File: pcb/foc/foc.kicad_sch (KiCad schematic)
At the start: 29 parts, among them J1 Conn_01x05_Pin, J2 Conn_01x03_Pin, Q1 BTN8982TA, Q2 BTN8982TA, Q3 BTN8982TA, U1 INA240A2PW, U2 INA240A2PW

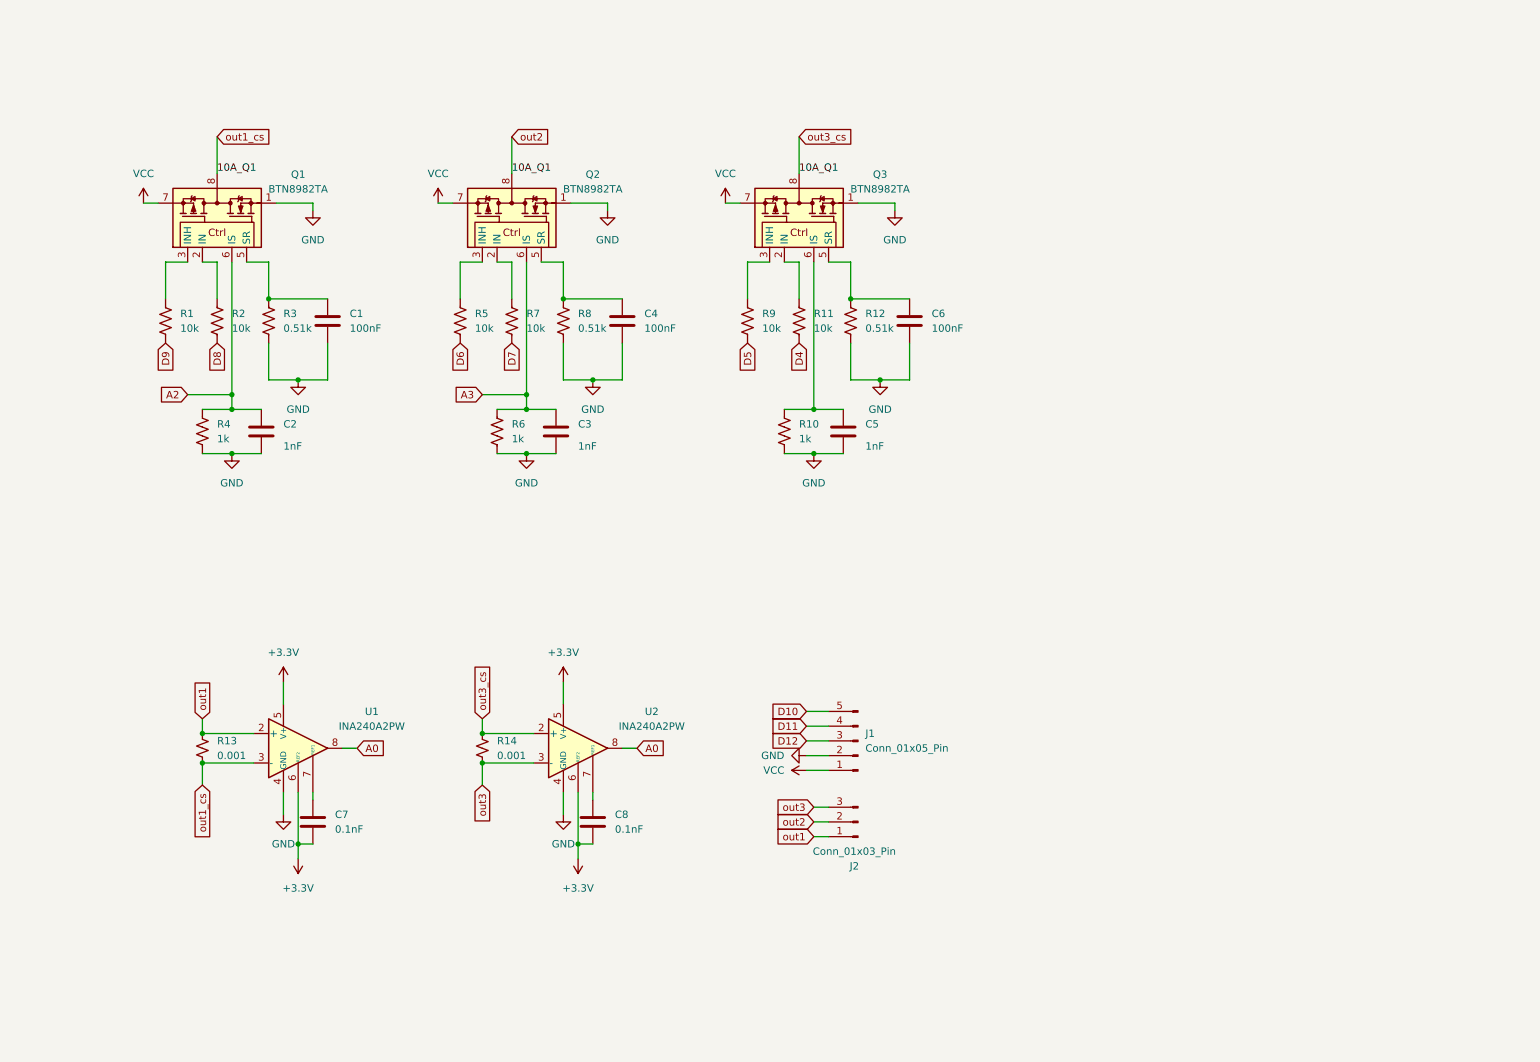
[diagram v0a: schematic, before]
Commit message: update foc board
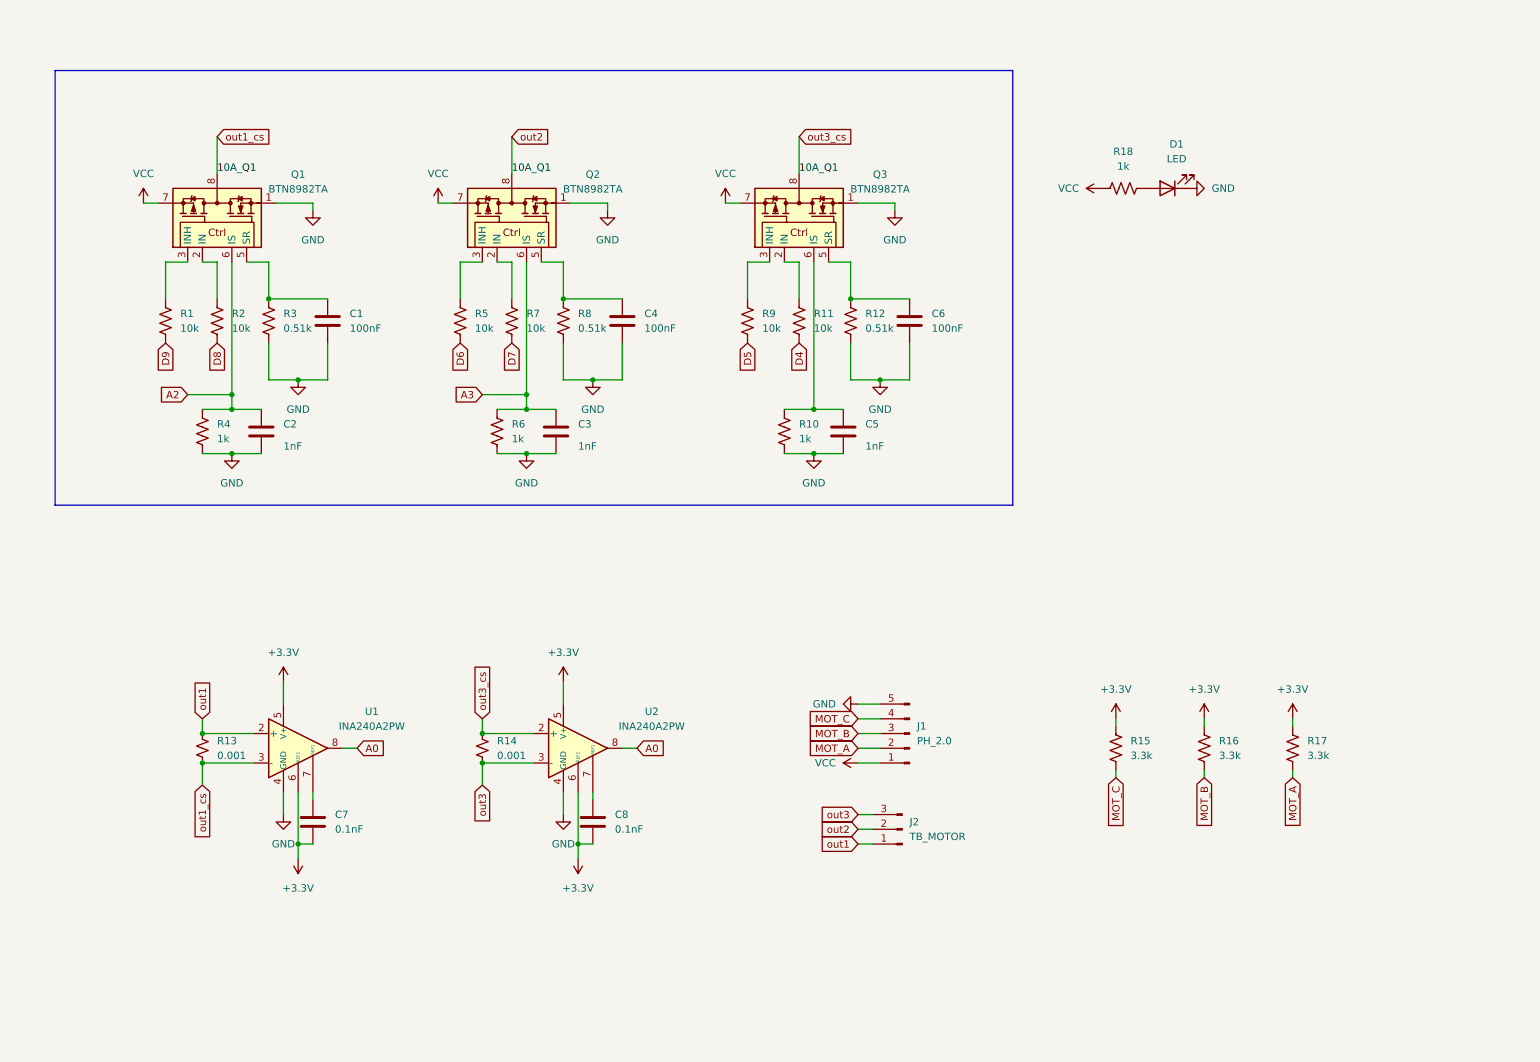
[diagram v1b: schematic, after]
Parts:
- added D1: LED, symbol Device:LED
- added R15, R16, R17: 3.3k, symbol Device:R_US
- added R18: 1k, symbol Device:R_US
- J1: value Conn_01x05_Pin -> PH_2.0
- J2: value Conn_01x03_Pin -> TB_MOTOR
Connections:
- net D10 is gone; now on net GND: J1.5 (Pin_5)
- net +3.3V: now also R15.1, R16.1, R17.1
- net GND: now also D1.1 (K); no longer J1.2 (Pin_2)
- net VCC: now also R18.1
- net D11 renamed MOT_C
- net MOT_C: now also R15.2
- net D12 renamed MOT_B
- net MOT_B: now also R16.2
- new net: D1.2 (A), R18.2
- new net MOT_A: J1.2 (Pin_2), R17.2
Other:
- moved on the sheet: J1, J2

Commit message: foc debug info designe
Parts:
- added D2: LED, symbol Device:LED
- added J3: Power42V, symbol Connector:Conn_01x02_Pin
- added J4, J7: Conn_01x05_Pin, symbol Connector:Conn_01x05_Pin
- added J5: Conn_01x04_Pin, symbol Connector:Conn_01x04_Pin
- added J6: Power3.3, symbol Connector:Conn_01x02_Pin
- added R22: 1k, symbol Device:R_US
- R13, R14: footprint (none) -> Resistor_SMD:R_2512_6332Metric
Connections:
- net +3.3V: now also R15.2, R16.2, J6.1 (Pin_1), R22.2; no longer R15.1, R16.1
- net A0: now also J5.4 (Pin_4); no longer U2.8
- net A2: now also J5.2 (Pin_2)
- net A3: now also J5.1 (Pin_1)
- net D4: now also J4.2 (Pin_2)
- net D5: now also J4.3 (Pin_3)
- net D6: now also J4.4 (Pin_4)
- net D7: now also J4.5 (Pin_5)
- net D8: now also J7.1 (Pin_1)
- net D9: now also J7.2 (Pin_2)
- net GND: now also D2.1 (K), J3.2 (Pin_2), J6.2 (Pin_2)
- net MOT_A: now also J7.3 (Pin_3)
- net MOT_B: now also R16.1, J7.4 (Pin_4); no longer R16.2
- net MOT_C: now also R15.1, J7.5 (Pin_5); no longer R15.2
- net VCC: now also J3.1 (Pin_1)
- net out1_cs: no longer J2.2 (Pin_2), Q2.4, Q2.8, Q3.4, Q3.8, R14.1, U2.2 (+)
- new net: D2.2 (A), R22.1
- new net A1: J5.3 (Pin_3), U2.8
- new net D3: J4.1 (Pin_1)
- new net out2: J2.2 (Pin_2), Q2.4, Q2.8
- new net out3_cs: Q3.4, Q3.8, R14.1, U2.2 (+)
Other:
- note added: "Debug info"
- note added: "current info"
- note added: "hall sensor pins"
- note added: "moto pins"
- note added: "power in and out"
- moved on the sheet: C1, C2, C3, C4, C5, C6, C7, C8, D1, J1, J2, Q1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

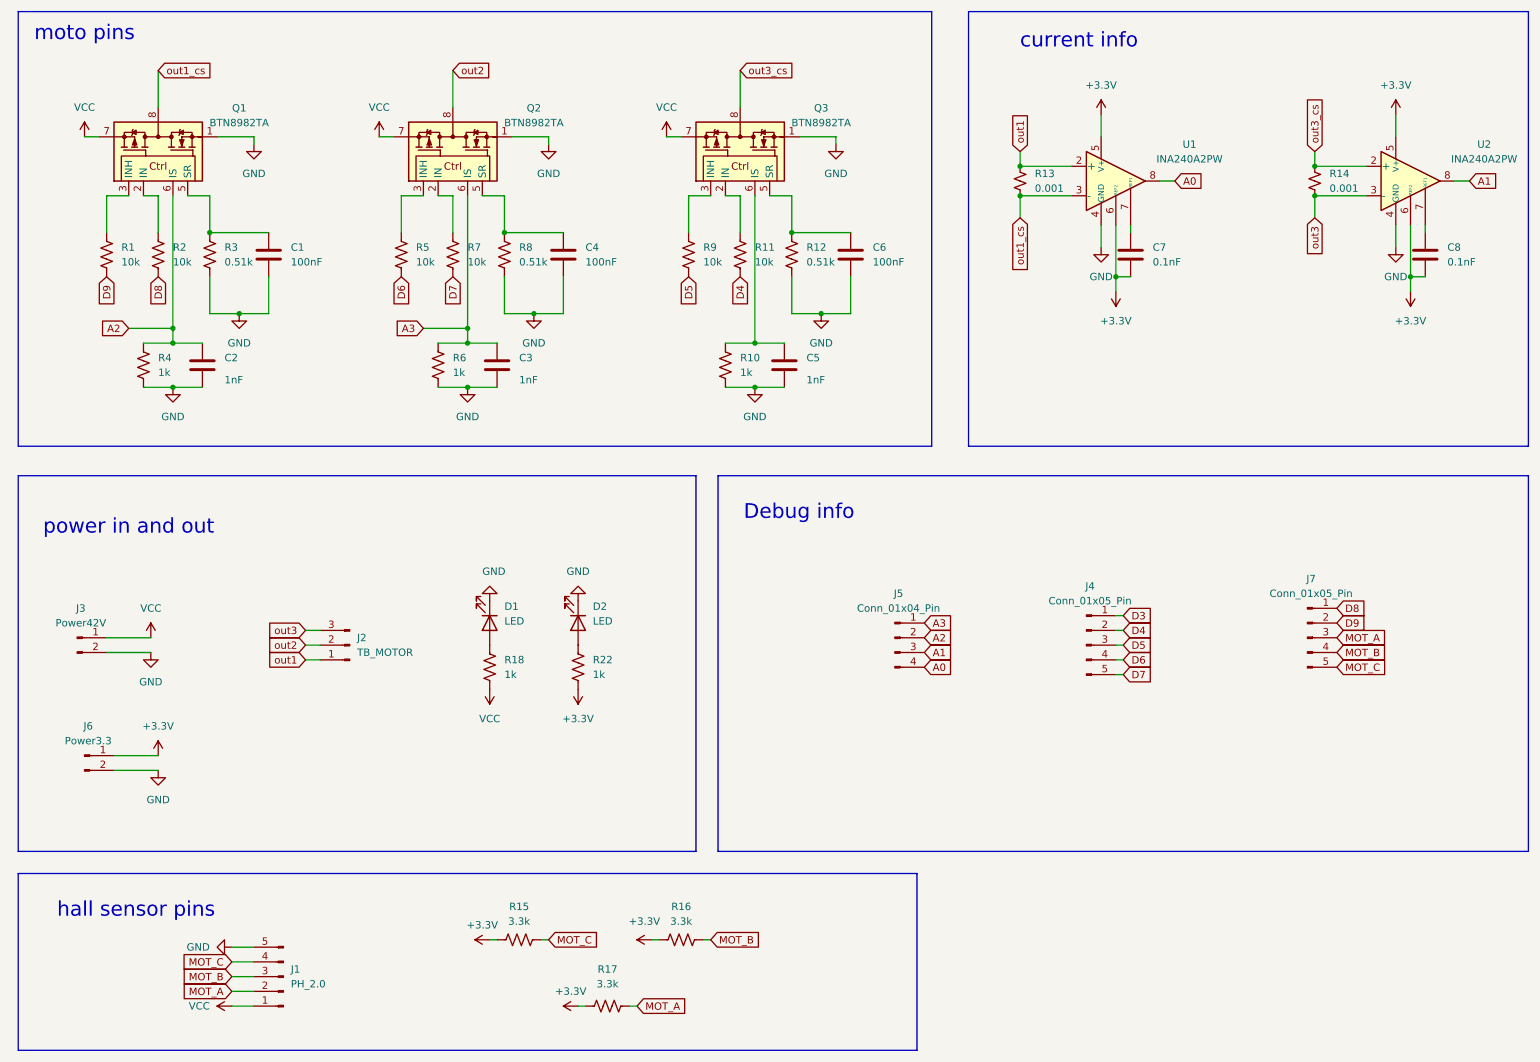
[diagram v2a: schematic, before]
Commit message: assign foot prints
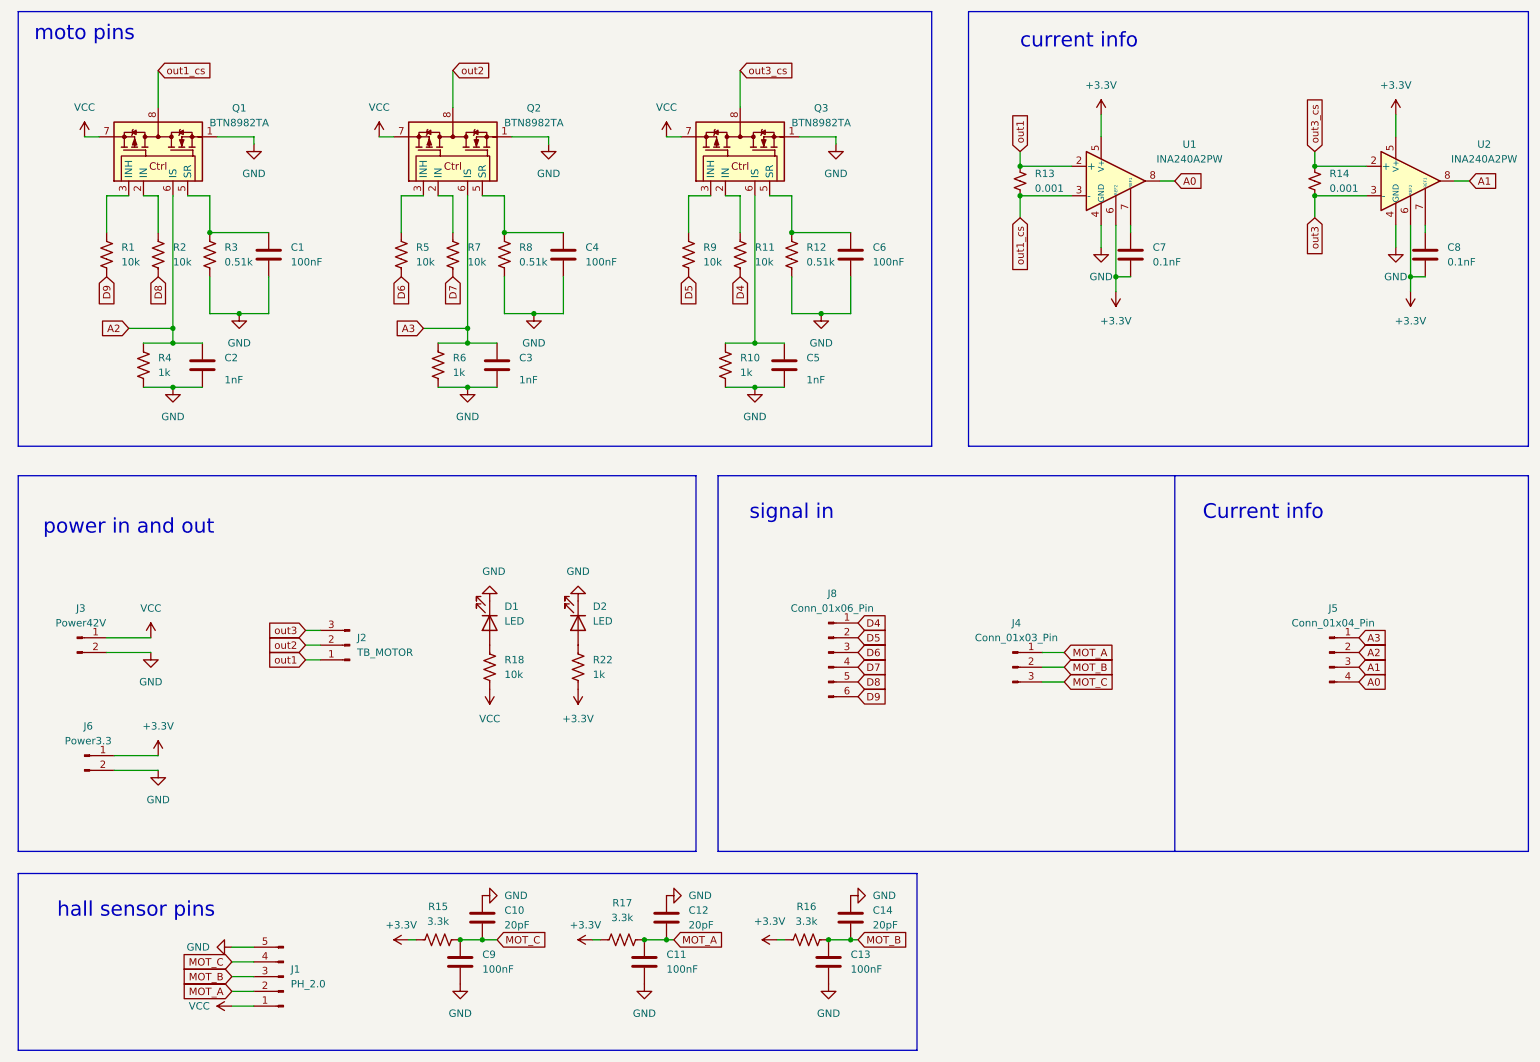
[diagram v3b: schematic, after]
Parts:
- removed J4, J7: Conn_01x05_Pin, symbol Connector:Conn_01x05_Pin
- added C10, C12, C14: 20pF, Capacitor_SMD:C_0603_1608Metric, symbol Device:C
- added C11, C13, C9: 100nF, Capacitor_SMD:C_0603_1608Metric, symbol Device:C
- added J4: Conn_01x03_Pin, Connector_PinHeader_2.54mm:PinHeader_1x03_P2.54mm_Vertical, symbol Connector:Conn_01x03_Pin
- added J8: Conn_01x06_Pin, Connector_PinHeader_2.54mm:PinHeader_1x06_P2.54mm_Vertical, symbol Connector:Conn_01x06_Pin
- C1, C2, C3, C4, C5, C6, C7, C8: footprint (none) -> Capacitor_SMD:C_0603_1608Metric
- D1, D2: footprint (none) -> LED_SMD:LED_0603_1608Metric
- J2: footprint Connector_JST:JST_PH_B3B-PH-SM4-TB_1x03-1MP_P2.00mm_Vertical -> Connector_AMASS:AMASS_MR30PW-M_1x03_P3.50mm_Horizontal
- J3: footprint (none) -> Connector_AMASS:AMASS_XT30PW-M_1x02_P2.50mm_Horizontal
- J5: footprint (none) -> Connector_PinHeader_2.54mm:PinHeader_1x04_P2.54mm_Vertical
- J6: footprint (none) -> Connector_PinHeader_1.27mm:PinHeader_1x02_P1.27mm_Vertical
- R1, R10, R11, R12, R15, R16, R17, R2, R22, R3, R4, R5, R6, R7, R8, R9: footprint (none) -> Resistor_SMD:R_0603_1608Metric
- R18: value 1k -> 10k; footprint (none) -> Resistor_SMD:R_0603_1608Metric
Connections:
- net D4: now also J8.1 (Pin_1)
- net D5: now also J8.2 (Pin_2)
- net D6: now also J8.3 (Pin_3)
- net D7: now also J8.4 (Pin_4)
- net D8: now also J8.5 (Pin_5)
- net D9: now also J8.6 (Pin_6)
- net GND: now also C10.1, C11.2, C12.1, C13.2, C14.1, C9.2
- net MOT_A: now also C11.1, C12.2, J4.1 (Pin_1)
- net MOT_B: now also C13.1, C14.2, J4.2 (Pin_2)
- net MOT_C: now also C10.2, C9.1, J4.3 (Pin_3)
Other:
- note added: "Current info"
- note added: "signal in"
- note removed: "Debug info"
- moved on the sheet: J5, R15, R16, R17

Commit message: 更新原理图和pcb
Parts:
- added NT1, NT2, NT3, NT4: NetTie_2, NetTie:NetTie-2_SMD_Pad2.0mm, symbol Device:NetTie_2
- 3.3v0: renamed from J6; footprint Connector_PinHeader_1.27mm:PinHeader_1x02_P1.27mm_Vertical -> Connector_PinHeader_2.54mm:PinHeader_1x02_P2.54mm_Vertical
- 42v0: renamed from J3; footprint Connector_AMASS:AMASS_XT30PW-M_1x02_P2.50mm_Horizontal -> Connector_AMASS:AMASS_XT60PW-M_1x02_P7.20mm_Horizontal
- current1: renamed from J5; value Conn_01x04_Pin -> current info
- hall1: renamed from J4; value Conn_01x03_Pin -> hall sig
- motor1: renamed from J8; value Conn_01x06_Pin -> sig in
- renumbered D2 to 3.3V1, D1 to 42V1
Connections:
- net +3.3V: now also J1.1 (Pin_1)
- net GND: now also 42v0.1 (Pin_1); no longer 42v0.2 (Pin_2)
- net VCC: now also 42v0.2 (Pin_2); no longer 42v0.1 (Pin_1), J1.1 (Pin_1)
- net out1: now also NT3.2; no longer R13.1, U1.2 (+)
- net out1_cs: now also NT4.2; no longer R13.2, U1.3 (-)
- net out3: now also NT2.1; no longer R14.2, U2.3 (-)
- net out3_cs: now also NT1.1; no longer R14.1, U2.2 (+)
- new net: NT3.1, R13.1, U1.2 (+)
- new net: NT4.1, R13.2, U1.3 (-)
- new net: NT1.2, R14.1, U2.2 (+)
- new net: NT2.2, R14.2, U2.3 (-)

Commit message: focV3 update
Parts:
- removed NT1, NT2, NT3, NT4: NetTie_2, NetTie:NetTie-2_SMD_Pad2.0mm, symbol Device:NetTie_2
- removed motor1: sig in, Connector_PinHeader_2.54mm:PinHeader_1x06_P2.54mm_Vertical, symbol Connector:Conn_01x06_Pin
- added C15: 330uf, Capacitor_SMD:CP_Elec_10x10.5, symbol Device:C_Polarized
- added motor1: input, Connector_PinHeader_2.54mm:PinHeader_1x03_P2.54mm_Vertical, symbol Connector:Conn_01x03_Pin
- added motor_en1: en_sig, Connector_PinHeader_2.54mm:PinHeader_1x03_P2.54mm_Vertical, symbol Connector:Conn_01x03_Pin
- hall1: value hall sig -> sig
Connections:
- net GND: now also C15.2
- net VCC: now also C15.1
- net out1: now also R13.1, U1.2 (+)
- net out1_cs: now also R13.2, U1.3 (-)
- net out3: now also R14.2, U2.3 (-)
- net out3_cs: now also R14.1, U2.2 (+)
- net D4 renamed IN_3
- net IN_3: now also motor1.3 (Pin_3)
- net D5 renamed INH_3
- net INH_3: now also motor_en1.3 (Pin_3)
- net D6 renamed INH_2
- net INH_2: now also motor_en1.2 (Pin_2)
- net D7 renamed IN_2
- net IN_2: now also motor1.2 (Pin_2)
- net D8 renamed IN_1
- net IN_1: now also motor1.1 (Pin_1)
- net D9 renamed INH_1
- net INH_1: now also motor_en1.1 (Pin_1)
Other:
- moved on the sheet: J2

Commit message: update pcb
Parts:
- added C16: 330uf, Capacitor_SMD:CP_Elec_10x10.5, symbol Device:C_Polarized
- motor_en1: footprint Connector_PinHeader_2.54mm:PinHeader_1x03_P2.54mm_Vertical -> Connector_PinHeader_2.54mm:PinHeader_1x02_P2.54mm_Vertical; symbol Connector:Conn_01x03_Pin -> Connector:Conn_01x02_Pin
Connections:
- net +3.3V: now also motor_en1.2 (Pin_2)
- net GND: now also C16.2
- net VCC: now also C16.1
- net INH_1 renamed INH_EN
- net INH_EN: now also R5.2, R9.2
- removed net INH_2: R5.2, motor_en1.2 (Pin_2)
- removed net INH_3: R9.2, motor_en1.3 (Pin_3)
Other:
- moved on the sheet: J2

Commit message: feat: update
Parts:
- removed 3.3V1, 42V1: LED, LED_SMD:LED_0603_1608Metric, symbol Device:LED
- removed 3.3v0: Power3.3, Connector_PinHeader_2.54mm:PinHeader_1x02_P2.54mm_Vertical, symbol Connector:Conn_01x02_Pin
- removed 42v0: Power42V, Connector_AMASS:AMASS_XT60PW-M_1x02_P7.20mm_Horizontal, symbol Connector:Conn_01x02_Pin
- removed motor_en1: en_sig, Connector_PinHeader_2.54mm:PinHeader_1x02_P2.54mm_Vertical, symbol Connector:Conn_01x02_Pin
- added 3.3V2, 42V2: LED, LED_SMD:LED_0603_1608Metric, symbol Device:LED
- renumbered C2 to C26, C1 to C27, C16 to C28, C15 to C29, C9 to C30, C10 to C31, C3 to C32, C4 to C33, C11 to C34, C12 to C35, C5 to C36, C13 to C37, C6 to C38, C14 to C39, C7 to C40, C8 to C41, J2 to J6, J1 to J7, Q1 to Q4, Q2 to Q5, Q3 to Q6, R1 to R27, R4 to R28, R2 to R29, R3 to R30, R5 to R31, R6 to R32, R15 to R33, R7 to R34, R18 to R35, R8 to R36, R22 to R37, R17 to R38, R9 to R39, R10 to R40, R11 to R41, R12 to R42, R16 to R43, R13 to R44, R14 to R45, U1 to U7, U2 to U8
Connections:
- net INH_EN is gone; now on net +3.3V: R27.2, R31.2, R39.2
- net GND: now also 3.3V2.1 (K), 42V2.1 (K)
- net at R35.2: now also 42V2.2 (A)
- net at R37.1: now also 3.3V2.2 (A)
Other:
- note added: "Current signal out"
- note added: "LMR16030SDDAR max input 60V but BTN8982TA max input 45V so final max VCC input is 45V"
- note added: "signal in and out"
- note removed: "Current info"
- note removed: "signal in"
- moved on the sheet: J6

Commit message: feat: update
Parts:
- removed current1: current info, Connector_PinHeader_2.54mm:PinHeader_1x04_P2.54mm_Vertical, symbol Connector:Conn_01x04_Pin
- removed hall1: sig, Connector_PinHeader_2.54mm:PinHeader_1x03_P2.54mm_Vertical, symbol Connector:Conn_01x03_Pin
- removed motor1: input, Connector_PinHeader_2.54mm:PinHeader_1x03_P2.54mm_Vertical, symbol Connector:Conn_01x03_Pin
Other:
- note removed: "Current signal out"
- note removed: "signal in and out"
